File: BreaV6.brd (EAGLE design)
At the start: 30.8 x 19 mm, 34 parts, among them J1 XF2L-0535-1, J2 XF2L-0535-1, Q1 ABM-16MHZ, SW1 LS12T2-T, SW2 EVQ11U09K, SW3 ESE31L11T, U2 TPS62200, X1 22-23-2021

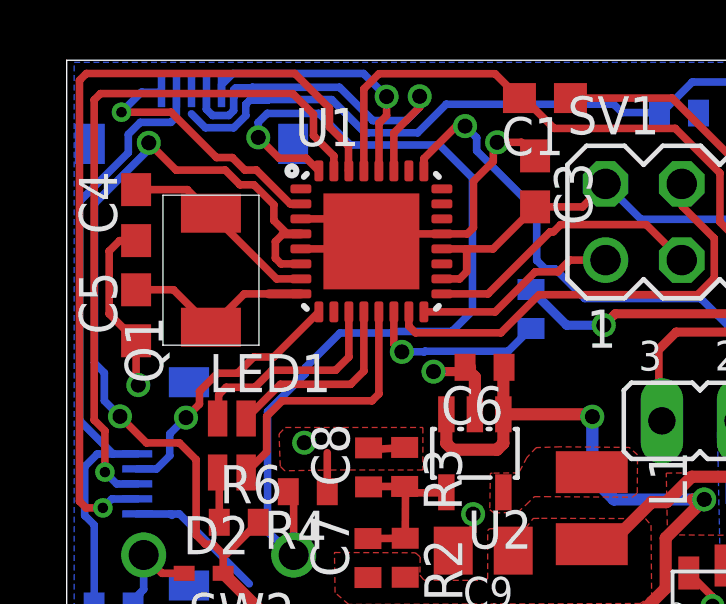
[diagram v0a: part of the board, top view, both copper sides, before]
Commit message: Brea V6   PwrSW and DetSW swap
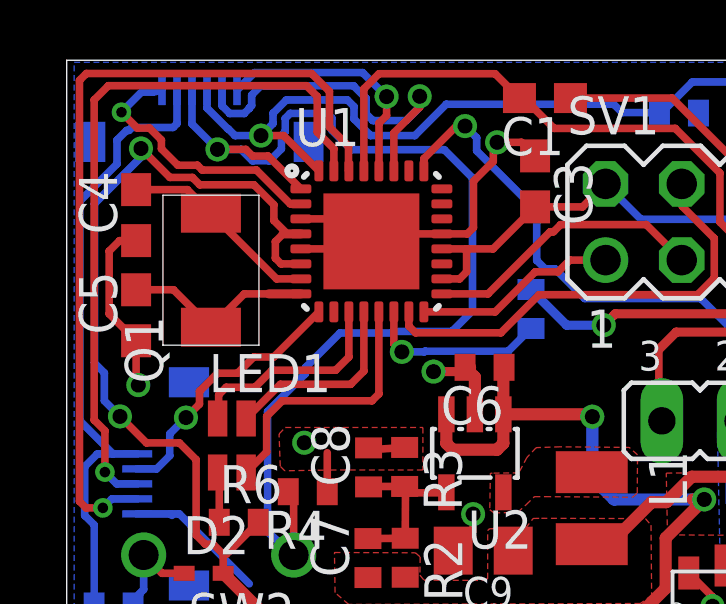
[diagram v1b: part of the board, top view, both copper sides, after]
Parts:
- removed J1: XF2L-0535-1, adafruit:XF2L-0535-1
- added J3: XF2L-0635-1, con-omron:XF2L-0635-1
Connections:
- removed net N$6: J1.3
- net DETSW: now also J3.3, U1.32
- net LEDSOC: now also J3.6; no longer J1.5
- net PWRSW: now also J3.4, U1.1; no longer U1.32
- net SCL: now also J3.1; no longer J1.1
- net SDA: now also J3.2; no longer J1.2
- net VBAT: now also J3.5; no longer J1.4
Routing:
- net PWRSW: track 31.3 -> 36.7 mm
- net DETSW: track 30.9 -> 34.0 mm, vias 0 -> 1
- net SCL: track 8.81 -> 8.14 mm
- net TX: track 23.6 -> 24.3 mm

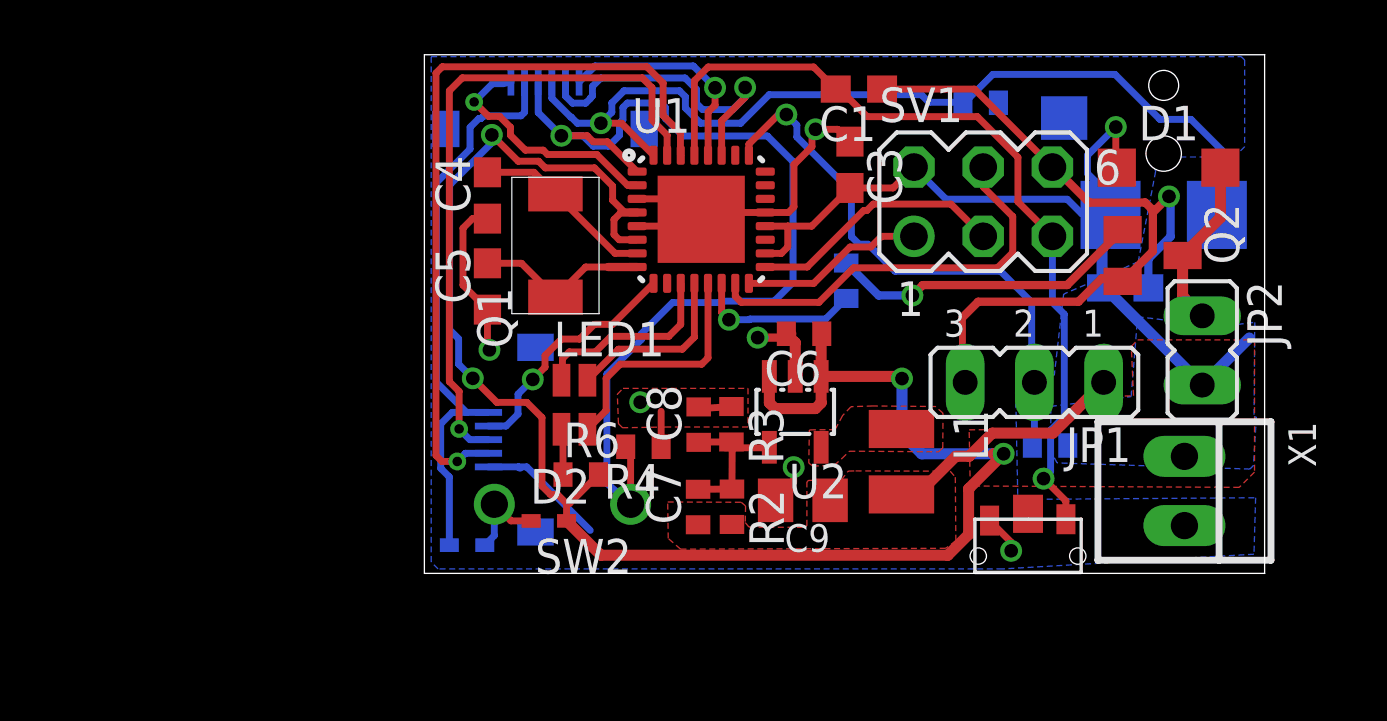
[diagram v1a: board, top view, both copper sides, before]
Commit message: To add signal control
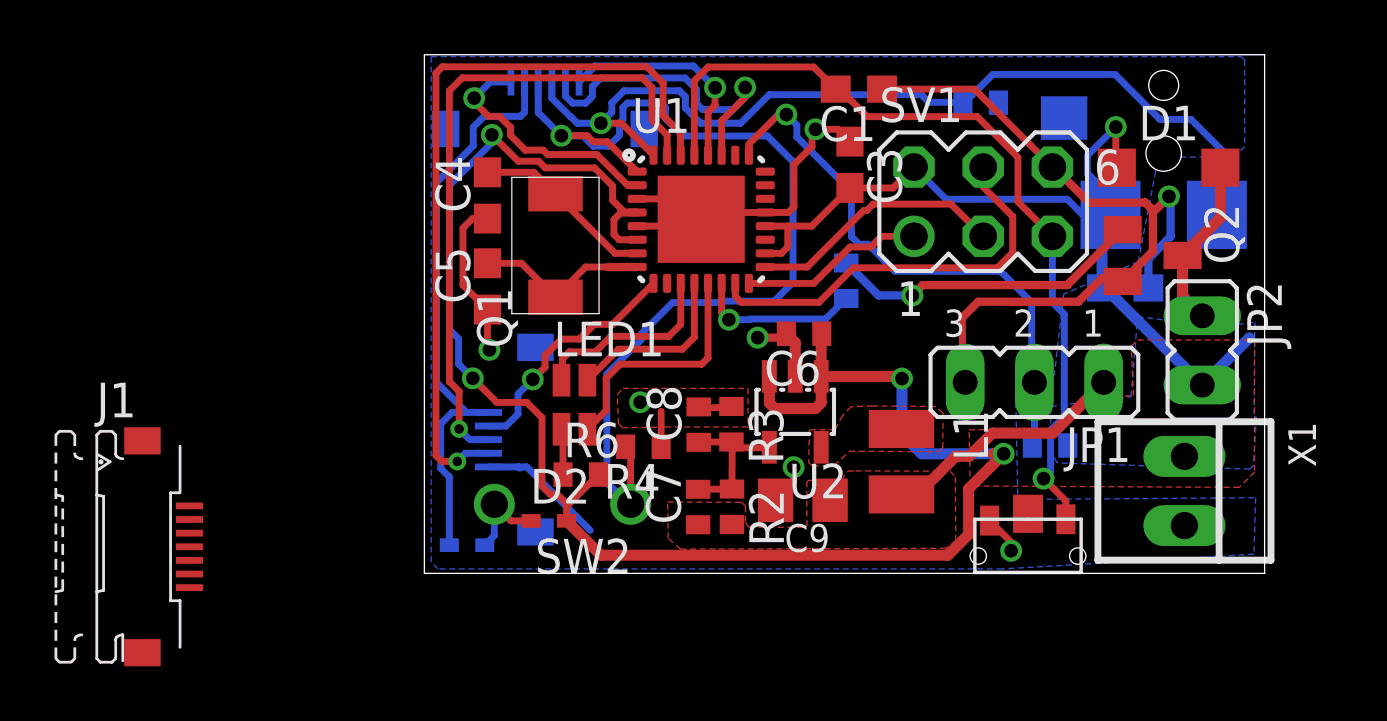
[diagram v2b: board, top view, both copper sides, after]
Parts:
- added J1: XF2L-0725-1, con-omron:XF2L-0725-1
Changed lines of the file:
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@@
 <attribute name="OC_NEWARK" value="05M1986" x="4.43" y="16.09" size="1.778" layer="28" rot="MR90" display="off"/>
+</element>
+<element name="J1" library="con-omron" library_urn="urn:adsk.eagle:library:167" package="XF2L-0725-1" package3d_urn="urn:adsk.eagle:package:9008/1" value="XF2L-0725-1" x="-10.52" y="0.94">
+<attribute name="MF" value="" x="-10.52" y="0.94" size="1.778" layer="27" display="off"/>
+<attribute name="MPN" value="XF2L-0725-1" x="-10.52" y="0.94" size="1.778" layer="27" display="off"/>
+<attribute name="OC_FARNELL" value="unknown" x="-10.52" y="0.94" size="1.778" layer="27" display="off"/>
+<attribute name="OC_NEWARK" value="37M0868" x="-10.52" y="0.94" size="1.778" layer="27" display="off"/>
 </element>
 </elements>
@@
 <signal name="LEDSOC">
 <contactref element="U1" pad="2"/>
-<via x="1.83" y="17.26" extent="1-16" drill="0.35"/>
-<wire x1="2.499" y1="17.929" x2="1.83" y2="17.26" width="0.254" layer="16"/>
+<via x="1.83" y="17.4" extent="1-16" drill="0.5"/>
 <wire x1="7.456525" y1="14.204" x2="7.81" y2="14.204" width="0.254" layer="1"/>
 <wire x1="6.328725" y1="15.3318" x2="7.456525" y2="14.204" width="0.254" layer="1"/>
 <contactref element="J3" pad="6"/>
-<wire x1="3.18" y1="17.995" x2="2.886" y2="17.929" width="0.254" layer="16"/>
-<wire x1="2.886" y1="17.929" x2="2.499" y2="17.929" width="0.254" layer="16"/>
-<wire x1="2.3582" y1="16.7318" x2="2.7624125" y2="16.7318" width="0.254" layer="1"/>
+<wire x1="2.7624125" y1="16.7318" x2="2.3582" y2="16.7318" width="0.254" layer="1"/>
 <wire x1="2.7624125" y1="16.7318" x2="3.1618" y2="16.3324125" width="0.254" layer="1"/>
 <wire x1="3.1618" y1="16.3324125" x2="3.1618" y2="16.0382" width="0.254" layer="1"/>
-<wire x1="1.83" y1="17.26" x2="2.3582" y2="16.7318" width="0.254" layer="1"/>
 <wire x1="4.362675" y1="15.4918" x2="4.522675" y2="15.3318" width="0.254" layer="1"/>
 <wire x1="3.7082" y1="15.4918" x2="4.362675" y2="15.4918" width="0.254" layer="1"/>
 <wire x1="3.1618" y1="16.0382" x2="3.7082" y2="15.4918" width="0.254" layer="1"/>
 <wire x1="4.522675" y1="15.3318" x2="6.328725" y2="15.3318" width="0.254" layer="1"/>
+<wire x1="1.83" y1="17.4" x2="2.425" y2="17.995" width="0.254" layer="16"/>
+<wire x1="2.425" y1="17.995" x2="3.18" y2="17.995" width="0.254" layer="16"/>
+<wire x1="2.3582" y1="16.7318" x2="1.83" y2="17.26" width="0.254" layer="1"/>
+<wire x1="1.83" y1="17.26" x2="1.83" y2="17.4" width="0.254" layer="1"/>
 </signal>
 <signal name="VBAT">
@@
 <wire x1="2.355" y1="5.87" x2="1.55" y2="5.87" width="0.254" layer="16"/>
 <wire x1="1.55" y1="5.87" x2="0.44" y2="6.98" width="0.254" layer="16"/>
-<wire x1="0.44" y1="6.98" x2="0.44" y2="14.2947375" width="0.254" layer="16"/>
+<wire x1="0.44" y1="14.2947375" x2="0.44" y2="6.98" width="0.254" layer="16"/>
 <wire x1="0.6032" y1="3.81865" x2="0.92" y2="3.50185" width="0.254" layer="16"/>
 <wire x1="0.92" y1="3.50185" x2="0.92" y2="1" width="0.254" layer="16"/>
@@
 <contactref element="J3" pad="5"/>
 <wire x1="3.68" y1="17.995" x2="3.68" y2="16.88" width="0.254" layer="16"/>
-<wire x1="3.55" y1="16.75" x2="3.68" y2="16.88" width="0.254" layer="16"/>
-<wire x1="0.44" y1="14.2947375" x2="1.68" y2="15.5347375" width="0.254" layer="16"/>
-<wire x1="1.68" y1="15.5347375" x2="1.68" y2="16.33" width="0.254" layer="16"/>
-<wire x1="1.68" y1="16.33" x2="2.0032" y2="16.6532" width="0.254" layer="16"/>
-<wire x1="2.0032" y1="16.6532" x2="2.08135" y2="16.6532" width="0.254" layer="16"/>
-<wire x1="2.08135" y1="16.6532" x2="2.17815" y2="16.75" width="0.254" layer="16"/>
-<wire x1="2.17815" y1="16.75" x2="3.55" y2="16.75" width="0.254" layer="16"/>
+<wire x1="2.1975875" y1="16.7318" x2="1.7982" y2="16.3324125" width="0.254" layer="16"/>
+<wire x1="3.5318" y1="16.7318" x2="2.1975875" y2="16.7318" width="0.254" layer="16"/>
+<wire x1="1.7982" y1="16.3324125" x2="1.7982" y2="15.6529375" width="0.254" layer="16"/>
+<wire x1="3.68" y1="16.88" x2="3.5318" y2="16.7318" width="0.254" layer="16"/>
+<wire x1="1.7982" y1="15.6529375" x2="0.44" y2="14.2947375" width="0.254" layer="16"/>
 </signal>
 <signal name="N$4">

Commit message: Final board files
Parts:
- removed J1: XF2L-0725-1, con-omron:XF2L-0725-1
- added X2: CON-1PINB, NewPart:CON-1PIN-B
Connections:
- new net SHUTDOWN_SIG: J3.6, U1.2
- net LEDSOC: now also U1.9, X2.P$1; no longer J3.6, U1.2
- net REST: now also U1.10; no longer U1.9
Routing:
- net SHUTDOWN_SIG: track 0.00 -> 7.72 mm, vias 0 -> 1
- net LEDSOC: track 9.15 -> 1.65 mm, vias 1 -> 0
- net REST: track 8.90 -> 10.4 mm
